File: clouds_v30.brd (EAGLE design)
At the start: 152.4 x 51.1 mm, 148 parts, among them IC1 74HC595D, IC10 TL072D, IC2 LM1117-3.3, IC3 MCP6002, IC4 MCP6004, IC5 STM32F405RGT6, IC6 LM4040B10, IC7 LM1117-3.3, IC8 WM8731, IC9 TL072D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

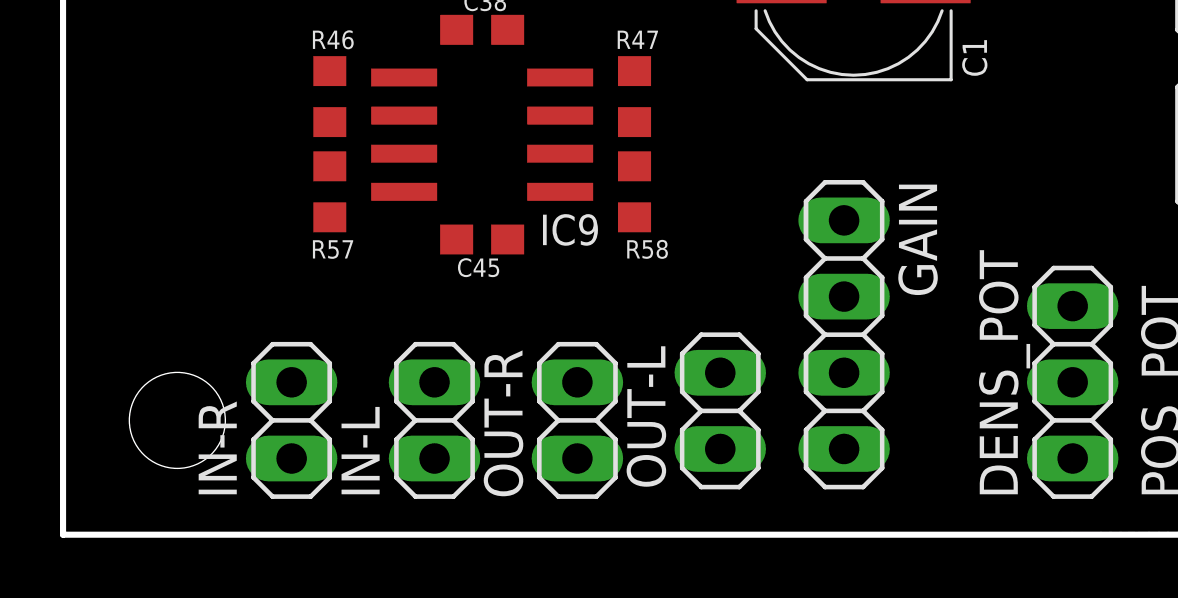
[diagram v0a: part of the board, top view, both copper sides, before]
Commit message: moved some stuff around on brd
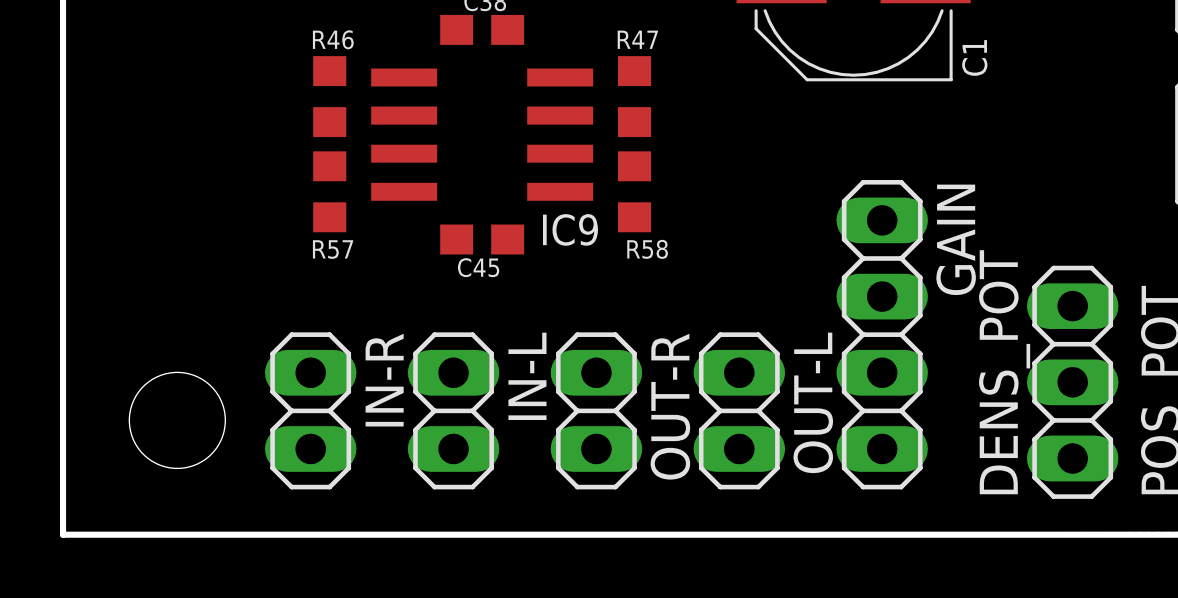
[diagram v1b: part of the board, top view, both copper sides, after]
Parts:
- moved GAIN 1.27 mm to (27.3, 6.67)
- moved OUT-R 0.71 mm to (17.8, 4.13), turned to 270 degrees
- moved IN-R 0.71 mm to (8.26, 4.13), turned to 270 degrees
- moved IN-L 0.71 mm to (13.0, 4.13), turned to 270 degrees
- moved OUT-L 0.64 mm to (22.5, 4.13), turned to 270 degrees
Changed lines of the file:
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@@
 <text x="144.145" y="18.415" size="1.27" layer="25" ratio="15" rot="R90">FTDI DONGLE</text>
 <text x="107.95" y="32.385" size="3.3528" layer="25" ratio="15">Clouds</text>
-<text x="97.4725" y="-12.065" size="3.175" layer="26" ratio="15" rot="MR0">Clouds</text>
+<text x="95.885" y="-6.0325" size="3.175" layer="26" ratio="15" rot="MR0">Clouds</text>
 <hole x="3.81" y="46.99" drill="3.2"/>
 <hole x="3.81" y="3.81" drill="3.2"/>
@@
 <attribute name="VALUE" x="112.0775" y="37.1475" size="0.6096" layer="27"/>
 </element>
-<element name="IN-R" library="pinhead" package="1X02" value="" x="7.62" y="3.81" rot="R90"/>
-<element name="IN-L" library="pinhead" package="1X02" value="" x="12.3825" y="3.81" rot="R90"/>
-<element name="GAIN" library="pinhead" package="1X04" value="" x="26.035" y="6.6675" rot="R270"/>
-<element name="OUT-R" library="pinhead" package="1X02" value="" x="17.145" y="3.81" rot="R90"/>
-<element name="OUT-L" library="pinhead" package="1X02" value="" x="21.9075" y="4.1275" rot="R90"/>
+<element name="IN-R" library="pinhead" package="1X02" value="" x="8.255" y="4.1275" rot="R270"/>
+<element name="IN-L" library="pinhead" package="1X02" value="" x="13.0175" y="4.1275" rot="R270"/>
+<element name="GAIN" library="pinhead" package="1X04" value="" x="27.305" y="6.6675" rot="R270"/>
+<element name="OUT-R" library="pinhead" package="1X02" value="" x="17.78" y="4.1275" rot="R270"/>
+<element name="OUT-L" library="pinhead" package="1X02" value="" x="22.5425" y="4.1275" rot="R270"/>
 <element name="POS_CV" library="pinhead" package="1X01" value="" x="128.5875" y="2.54" rot="R90"/>
 <element name="V_OCT" library="pinhead" package="1X01" value="" x="113.665" y="2.54" rot="R90"/>
@@
 <wire x1="33.655" y1="7.62" x2="28.7525" y2="18.415" width="0" layer="19" extent="1-1"/>
 <wire x1="39.0525" y1="7.62" x2="33.655" y2="7.62" width="0" layer="19" extent="1-1"/>
-<wire x1="21.9075" y1="5.3975" x2="33.655" y2="7.62" width="0" layer="19" extent="1-1"/>
-<wire x1="17.145" y1="5.08" x2="21.9075" y2="5.3975" width="0" layer="19" extent="1-1"/>
-<wire x1="12.3825" y1="5.08" x2="17.145" y2="5.08" width="0" layer="19" extent="1-1"/>
-<wire x1="7.62" y1="5.08" x2="12.3825" y2="5.08" width="0" layer="19" extent="1-1"/>
-<wire x1="14.82" y1="9.8425" x2="17.145" y2="5.08" width="0" layer="19" extent="1-1"/>
+<wire x1="22.5425" y1="2.8575" x2="33.655" y2="7.62" width="0" layer="19" extent="1-1"/>
+<wire x1="17.78" y1="2.8575" x2="22.5425" y2="2.8575" width="0" layer="19" extent="1-1"/>
+<wire x1="13.0175" y1="2.8575" x2="17.78" y2="2.8575" width="0" layer="19" extent="1-1"/>
+<wire x1="8.255" y1="2.8575" x2="13.0175" y2="2.8575" width="0" layer="19" extent="1-1"/>
+<wire x1="14.82" y1="9.8425" x2="17.78" y2="2.8575" width="0" layer="19" extent="1-1"/>
 <wire x1="16.57" y1="11.43" x2="14.82" y2="9.8425" width="0" layer="19" extent="1-1"/>
 <wire x1="11.37" y1="12.7" x2="14.82" y2="9.8425" width="0" layer="19" extent="1-1"/>
@@
 <wire x1="102.6088" y1="43.815" x2="86.855" y2="44.7675" width="0" layer="19" extent="1-1"/>
 <wire x1="108.8463" y1="43.815" x2="102.6088" y2="43.815" width="0" layer="19" extent="1-1"/>
-<wire x1="11.43" y1="47.625" x2="7.62" y2="5.08" width="0" layer="19" extent="1-1"/>
+<wire x1="11.43" y1="47.625" x2="8.255" y2="2.8575" width="0" layer="19" extent="1-1"/>
 </signal>
 <signal name="N$7">
@@
 <contactref element="R58" pad="2"/>
 <contactref element="IN-R" pad="1"/>
-<wire x1="7.62" y1="2.54" x2="19.05" y2="10.58" width="0" layer="19" extent="1-1"/>
+<wire x1="8.255" y1="5.3975" x2="19.05" y2="10.58" width="0" layer="19" extent="1-1"/>
 </signal>
 <signal name="N$18">
@@
 <contactref element="R62" pad="1"/>
 <contactref element="OUT-R" pad="1"/>
-<wire x1="17.145" y1="2.54" x2="87.415" y2="29.845" width="0" layer="19" extent="1-1"/>
+<wire x1="17.78" y1="5.3975" x2="87.415" y2="29.845" width="0" layer="19" extent="1-1"/>
 </signal>
 <signal name="N$31">
@@
 <contactref element="R61" pad="1"/>
 <contactref element="OUT-L" pad="1"/>
-<wire x1="21.9075" y1="2.8575" x2="79.795" y2="26.9875" width="0" layer="19" extent="1-1"/>
+<wire x1="22.5425" y1="5.3975" x2="79.795" y2="26.9875" width="0" layer="19" extent="1-1"/>
 </signal>
 <signal name="N$14">
@@
 <contactref element="R53" pad="2"/>
 <contactref element="GAIN" pad="2"/>
-<wire x1="26.035" y1="7.9375" x2="119.0625" y2="10.8975" width="0" layer="19" extent="1-1"/>
-<wire x1="16.57" y1="13.97" x2="26.035" y2="7.9375" width="0" layer="19" extent="1-1"/>
+<wire x1="27.305" y1="7.9375" x2="119.0625" y2="10.8975" width="0" layer="19" extent="1-1"/>
+<wire x1="16.57" y1="13.97" x2="27.305" y2="7.9375" width="0" layer="19" extent="1-1"/>
 </signal>
 <signal name="N$51">
@@
 <contactref element="R55" pad="2"/>
 <contactref element="GAIN" pad="3"/>
-<wire x1="26.035" y1="5.3975" x2="123.825" y2="10.8975" width="0" layer="19" extent="1-1"/>
-<wire x1="11.37" y1="15.24" x2="26.035" y2="5.3975" width="0" layer="19" extent="1-1"/>
+<wire x1="27.305" y1="5.3975" x2="123.825" y2="10.8975" width="0" layer="19" extent="1-1"/>
+<wire x1="11.37" y1="15.24" x2="27.305" y2="5.3975" width="0" layer="19" extent="1-1"/>
 </signal>
 <signal name="N$52">
 <contactref element="R47" pad="1"/>
 <contactref element="GAIN" pad="1"/>
-<wire x1="19.05" y1="15.455" x2="26.035" y2="10.4775" width="0" layer="19" extent="1-1"/>
+<wire x1="19.05" y1="15.455" x2="27.305" y2="10.4775" width="0" layer="19" extent="1-1"/>
 </signal>
 <signal name="N$53">
 <contactref element="R46" pad="1"/>
 <contactref element="GAIN" pad="4"/>
-<wire x1="8.89" y1="15.455" x2="26.035" y2="2.8575" width="0" layer="19" extent="1-1"/>
+<wire x1="8.89" y1="15.455" x2="27.305" y2="2.8575" width="0" layer="19" extent="1-1"/>
 </signal>
 <signal name="N$54">
@@
 <contactref element="R57" pad="2"/>
 <contactref element="IN-L" pad="1"/>
-<wire x1="12.3825" y1="2.54" x2="8.89" y2="10.58" width="0" layer="19" extent="1-1"/>
+<wire x1="13.0175" y1="5.3975" x2="8.89" y2="10.58" width="0" layer="19" extent="1-1"/>
 </signal>
 <signal name="PITCH_POT">

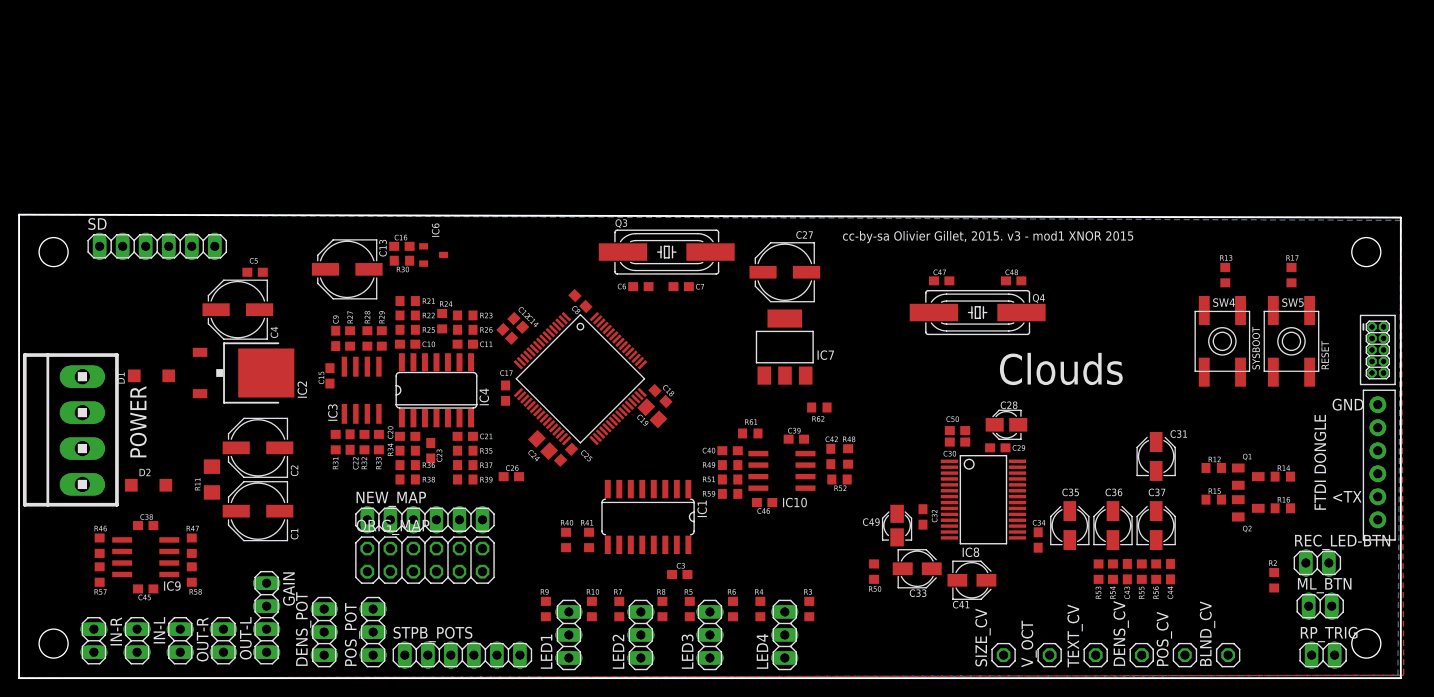
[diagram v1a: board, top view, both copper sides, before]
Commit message: moving stuff around, think i should move the i2s interface
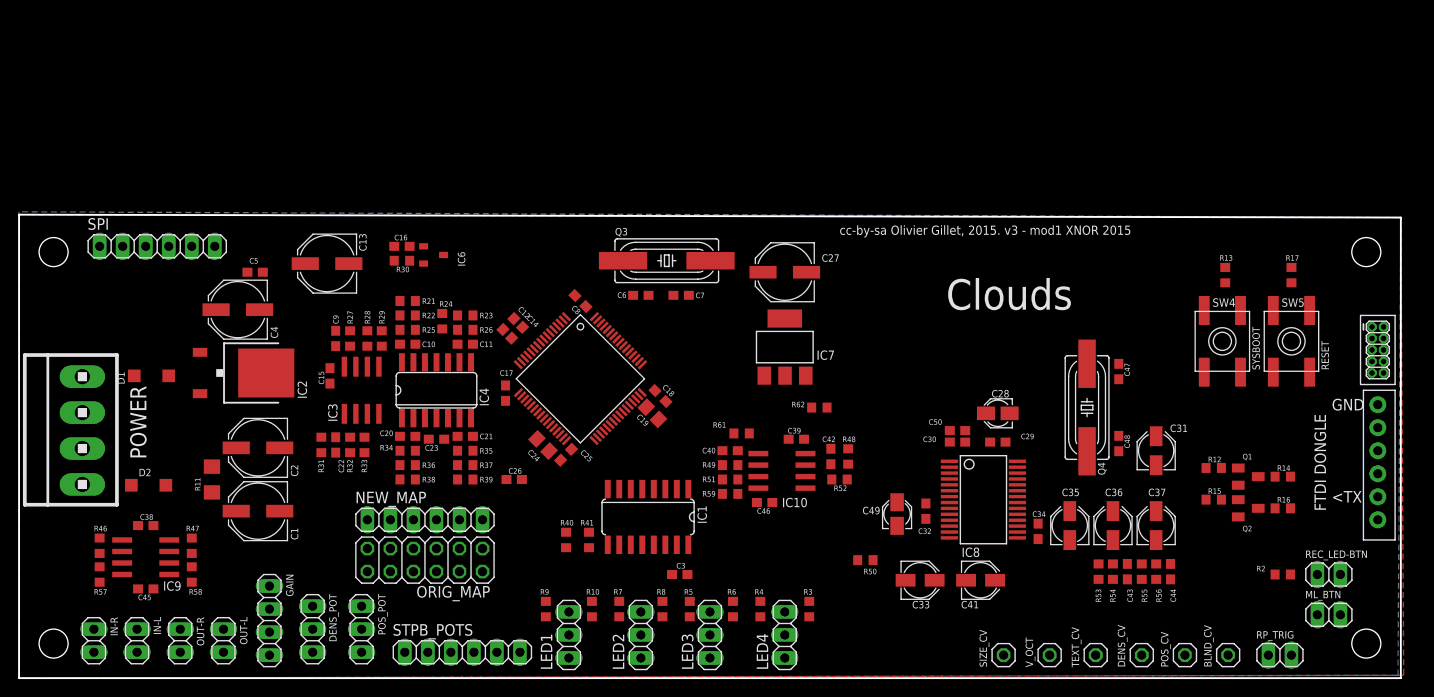
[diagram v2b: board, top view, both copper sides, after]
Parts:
- moved C47 21.9 mm to (121.3, 33.8), turned to 90 degrees
- moved C48 21.4 mm to (121.3, 25.9), turned to 270 degrees
- moved Q4 16.0 mm to (117.8, 29.8), turned to 270 degrees
- moved RP_TRIG 4.76 mm to (139.1, 2.54)
- moved C13 2.31 mm to (34.0, 45.7)
- moved REC_LED-BTN 1.80 mm to (144.5, 11.4)
- moved C22 1.62 mm to (34.9, 25.7)
- moved R31 1.62 mm to (33.3, 25.7)
- moved R32 1.62 mm to (36.5, 25.7)
- moved R33 1.62 mm to (38.1, 25.7)
- moved C28 1.59 mm to (108.0, 29.2)
- moved R50 1.59 mm to (93.3, 13.0), turned to 180 degrees
- moved C23 1.42 mm to (46.0, 26.4), turned to 180 degrees
- moved ML_BTN 1.35 mm to (144.5, 6.99)
- moved DENS_POT 1.31 mm to (32.4, 5.40), turned to 270 degrees
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- renumbered SD to SPI

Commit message: moved i2s closer to audio i/o
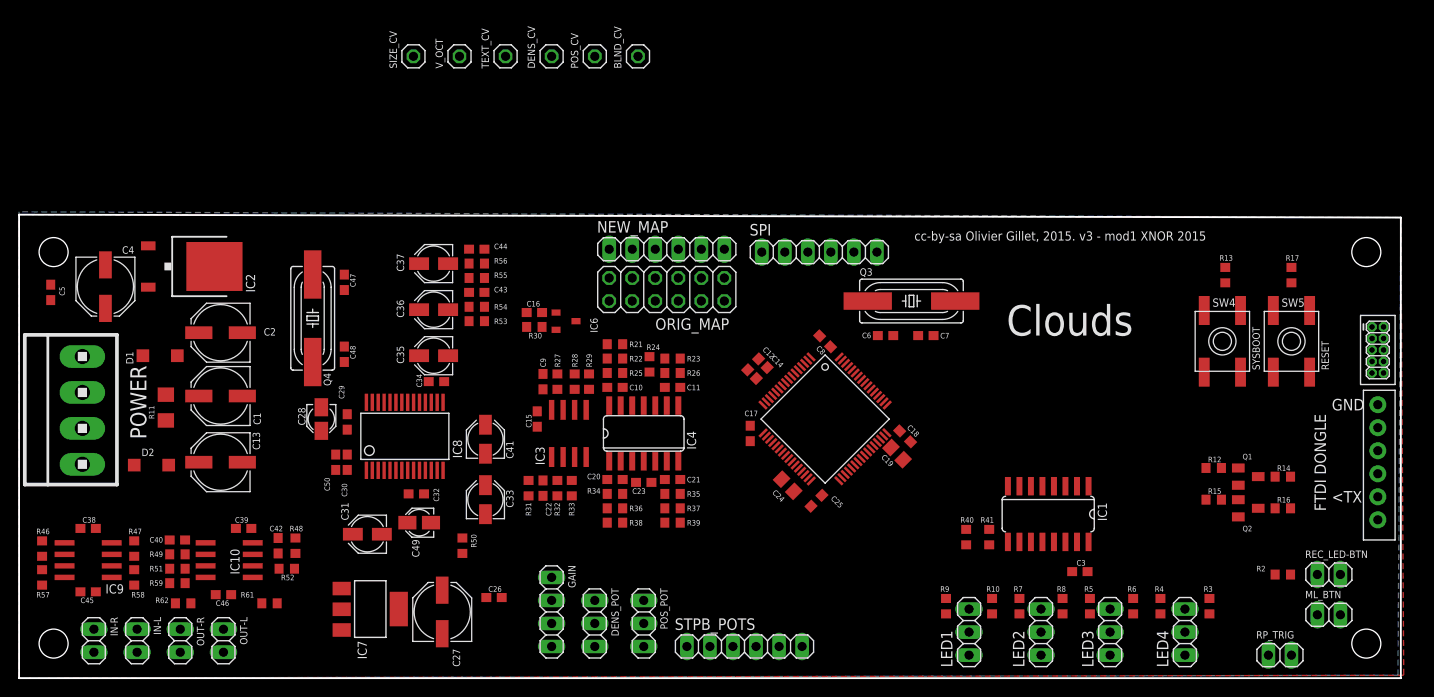
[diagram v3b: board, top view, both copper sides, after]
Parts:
- moved DENS_CV 92.7 mm to (58.7, 68.6)
- moved POS_CV 92.7 mm to (63.5, 68.6)
- moved TEXT_CV 92.7 mm to (53.7, 68.6)
- moved V_OCT 92.7 mm to (48.6, 68.6)
- moved BLND_CV 92.7 mm to (68.3, 68.6)
- moved SIZE_CV 92.7 mm to (43.5, 68.6)
- moved C31 87.5 mm to (38.4, 15.9), turned to 180 degrees
- moved C47 86.0 mm to (35.9, 43.7)
- moved C48 86.0 mm to (35.9, 35.7)
- moved Q4 86.0 mm to (32.4, 39.7)
- moved C37 84.8 mm to (45.7, 45.7), turned to 180 degrees
- moved C44 84.4 mm to (50.5, 47.3), turned to 0 degrees
- moved R56 82.3 mm to (50.5, 45.7), turned to 180 degrees
- moved R55 80.2 mm to (50.5, 44.1), turned to 0 degrees
- moved C36 78.6 mm to (45.7, 40.6), turned to 180 degrees
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
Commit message: about to route
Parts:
- moved BLND_CV 73.0 mm to (99.4, 2.54)
- moved DENS_CV 73.0 mm to (89.9, 2.54)
- moved POS_CV 73.0 mm to (94.6, 2.54)
- moved SIZE_CV 73.0 mm to (74.6, 2.54)
- moved TEXT_CV 73.0 mm to (84.8, 2.54)
- moved V_OCT 73.0 mm to (79.7, 2.54)
- moved STPB_POTS 12.4 mm to (68.9, 8.89), turned to 90 degrees
- moved Q1 9.04 mm to (138.4, 13.7)
- moved Q2 9.04 mm to (138.4, 10.2)
- moved R14 9.04 mm to (142.2, 13.7)
- moved R16 9.04 mm to (142.2, 10.2)
- moved R12 9.04 mm to (134.6, 14.6)
- moved R15 9.04 mm to (134.6, 11.1)
- moved R2 6.61 mm to (144.8, 7.62)
- moved DENS_POT 6.42 mm to (57.1, 5.08)
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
